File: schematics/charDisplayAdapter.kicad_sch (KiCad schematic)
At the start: 3 parts, among them J16 port, U15 lcdCharScreen

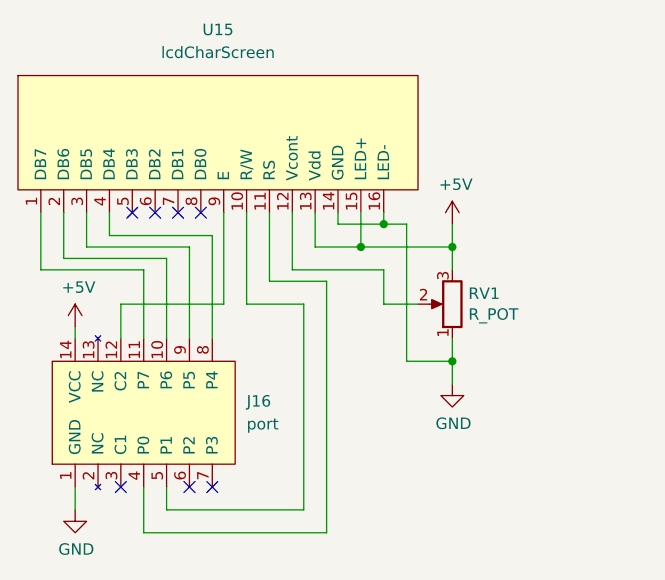
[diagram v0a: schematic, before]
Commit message: Fix errors in schematics
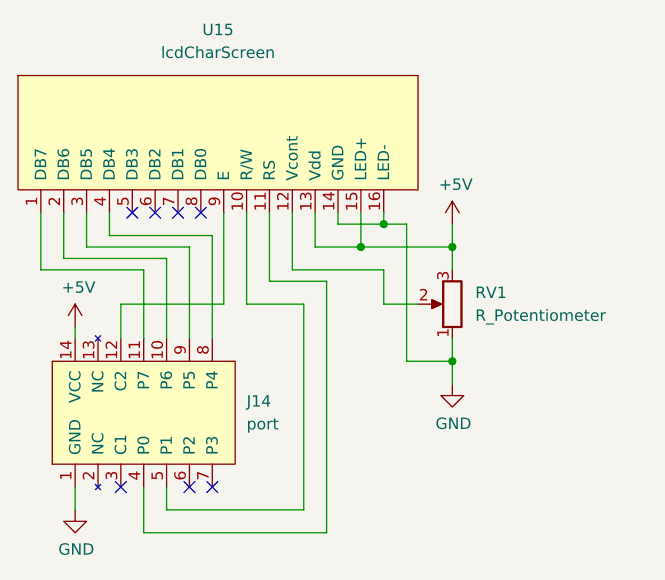
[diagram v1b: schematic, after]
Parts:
- removed RV1: R_POT, symbol Device:R_POT
- added RV1: R_Potentiometer, symbol Device:R_Potentiometer
- renumbered J16 to J14
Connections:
- net +5V: now also RV1.3
- net GND: now also RV1.1
- net at U15.12 (Vcont): now also RV1.2
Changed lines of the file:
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@@
 		(on_board yes)
 		(dnp no)
-		(property "Reference" "#PWR081"
+		(property "Reference" "#PWR073"
 			(at 60.96 106.68 0)
 			(effects
@@
 			(project "markus"
 				(path "/03a78ca6-eaff-4f05-be7b-36cd15f8b56d/a0bf404f-668b-4484-930f-14496d1755c9"
-					(reference "#PWR081")
+					(reference "#PWR073")
 					(unit 1)
 				)
@@
 		(dnp no)
 		(fields_autoplaced yes)
-		(property "Reference" "J16"
+		(property "Reference" "J14"
 			(at 80.01 88.2649 90)
 			(effects
@@
 			(project ""
 				(path "/03a78ca6-eaff-4f05-be7b-36cd15f8b56d/a0bf404f-668b-4484-930f-14496d1755c9"
-					(reference "J16")
+					(reference "J14")
 					(unit 1)
 				)
@@
 		(on_board yes)
 		(dnp no)
-		(property "Reference" "#PWR082"
+		(property "Reference" "#PWR074"
 			(at 102.87 72.39 0)
 			(effects
@@
 			(project "markus"
 				(path "/03a78ca6-eaff-4f05-be7b-36cd15f8b56d/a0bf404f-668b-4484-930f-14496d1755c9"
-					(reference "#PWR082")
+					(reference "#PWR074")
 					(unit 1)
 				)
@@
 	)
 	(symbol
-		(lib_id "Device:R_POT")
+		(lib_id "Device:R_Potentiometer")
 		(at 102.87 77.47 180)
 		(unit 1)
@@
 		(on_board yes)
 		(dnp no)
+		(fields_autoplaced yes)
 		(property "Reference" "RV1"
-			(at 104.648 76.3016 0)
+			(at 105.41 76.1999 0)
 			(effects
 				(font
@@
 			)
 		)
-		(property "Value" "R_POT"
-			(at 104.648 78.613 0)
+		(property "Value" "R_Potentiometer"
+			(at 105.41 78.7399 0)
 			(effects
 				(font
@@
 			)
 		)
-		(property "Description" ""
+		(property "Description" "Potentiometer"
 			(at 102.87 77.47 0)
 			(effects
@@
 		(pin "1"
 		)
+		(pin "3"
+		)
 		(pin "2"
 		)
-		(pin "3"
-		)
-		(instances
-			(project "markus"
+		(instances
+			(project ""
 				(path "/03a78ca6-eaff-4f05-be7b-36cd15f8b56d/a0bf404f-668b-4484-930f-14496d1755c9"
 					(reference "RV1")
@@
 		(on_board yes)
 		(dnp no)
-		(property "Reference" "#PWR080"
+		(property "Reference" "#PWR072"
 			(at 60.96 83.82 0)
 			(effects
@@
 			(project "markus"
 				(path "/03a78ca6-eaff-4f05-be7b-36cd15f8b56d/a0bf404f-668b-4484-930f-14496d1755c9"
-					(reference "#PWR080")
+					(reference "#PWR072")
 					(unit 1)
 				)
@@
 		(on_board yes)
 		(dnp no)
-		(property "Reference" "#PWR083"
+		(property "Reference" "#PWR075"
 			(at 102.87 92.71 0)
 			(effects
@@
 			(project "markus"
 				(path "/03a78ca6-eaff-4f05-be7b-36cd15f8b56d/a0bf404f-668b-4484-930f-14496d1755c9"
-					(reference "#PWR083")
-					(unit 1)
-				)
+					(reference "#PWR075")
+					(unit 1)
+				)
